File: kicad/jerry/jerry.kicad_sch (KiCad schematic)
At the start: 33 parts, among them J1 Conn_01x06_Socket, U1 NE555P, U10 74LS08, U2 74LS393, U3 74HC595, U4 74LS266, U5 74HC74, U6 74HC04, U7 74LS21, U8 NE555P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

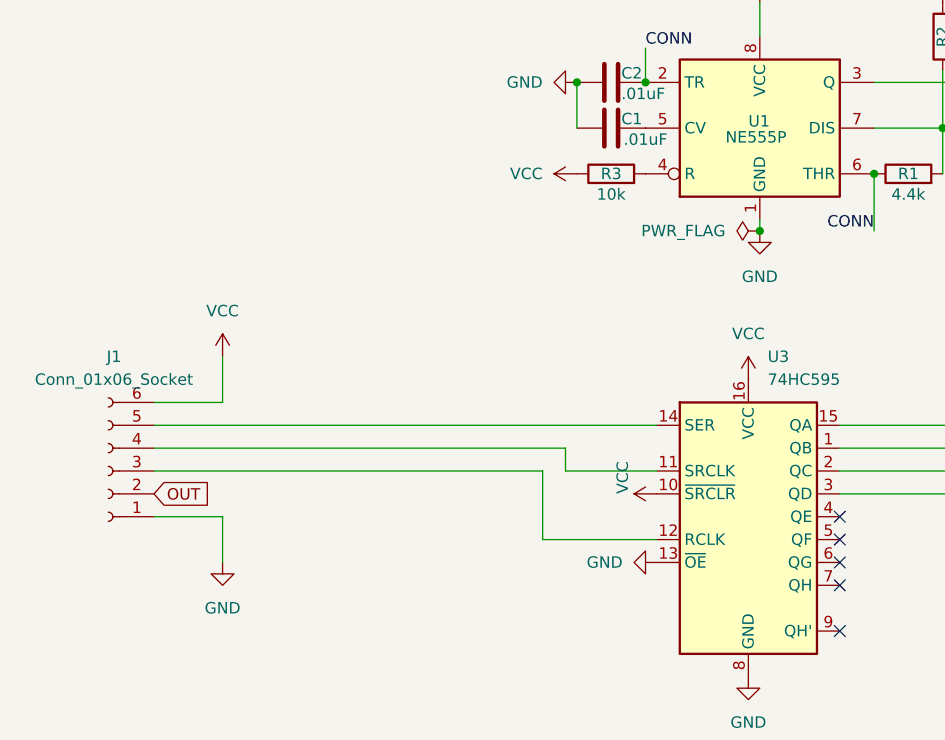
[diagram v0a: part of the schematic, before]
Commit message: updated pcb schematic
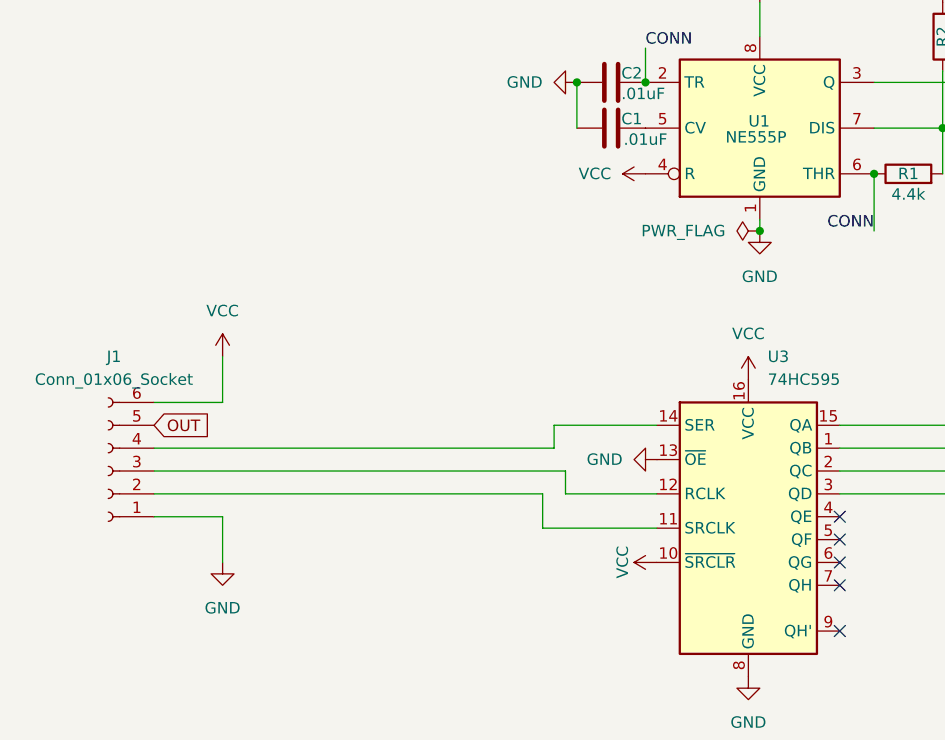
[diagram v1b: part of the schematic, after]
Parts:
- removed R3: 10k, Resistor_SMD:R_0603_1608Metric, symbol Device:R
- J1: footprint Connector_PinSocket_2.54mm:PinSocket_2x03_P2.54mm_Vertical -> Connector_PinHeader_2.54mm:PinHeader_1x06_P2.54mm_Vertical
- U1, U8: footprint Package_DIP:DIP-8_W7.62mm -> Package_SO:SO-8_3.9x4.9mm_P1.27mm
- U10, U2, U4, U5, U6, U7, U9: footprint Package_DIP:DIP-14_W7.62mm -> Package_SO:SO-14_3.9x8.65mm_P1.27mm
- U3: footprint Package_DIP:DIP-16_W7.62mm -> Package_SO:SO-16_3.9x9.9mm_P1.27mm
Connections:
- net OUT: now also J1.5 (Pin_5); no longer J1.2 (Pin_2)
- net VCC: now also U1.4 (R)
- net at U3.11 (SRCLK): now also J1.2 (Pin_2); no longer J1.4 (Pin_4)
- net at U3.14 (SER): now also J1.4 (Pin_4); no longer J1.5 (Pin_5)
